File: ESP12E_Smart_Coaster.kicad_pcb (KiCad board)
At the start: 2 copper layers, 110.7 x 110.7 mm, 49 parts, among them J1 SPI_Header, J2 MLX90614 Temp Sensor, J3 Programming_header, J4 Power_Input_Header, Q1 SI2302, SW1 SW_SPDT, SW2 SW_Push, U1 T6845C_Module, U2 AMS1117-3.3, U3 ESP-12E

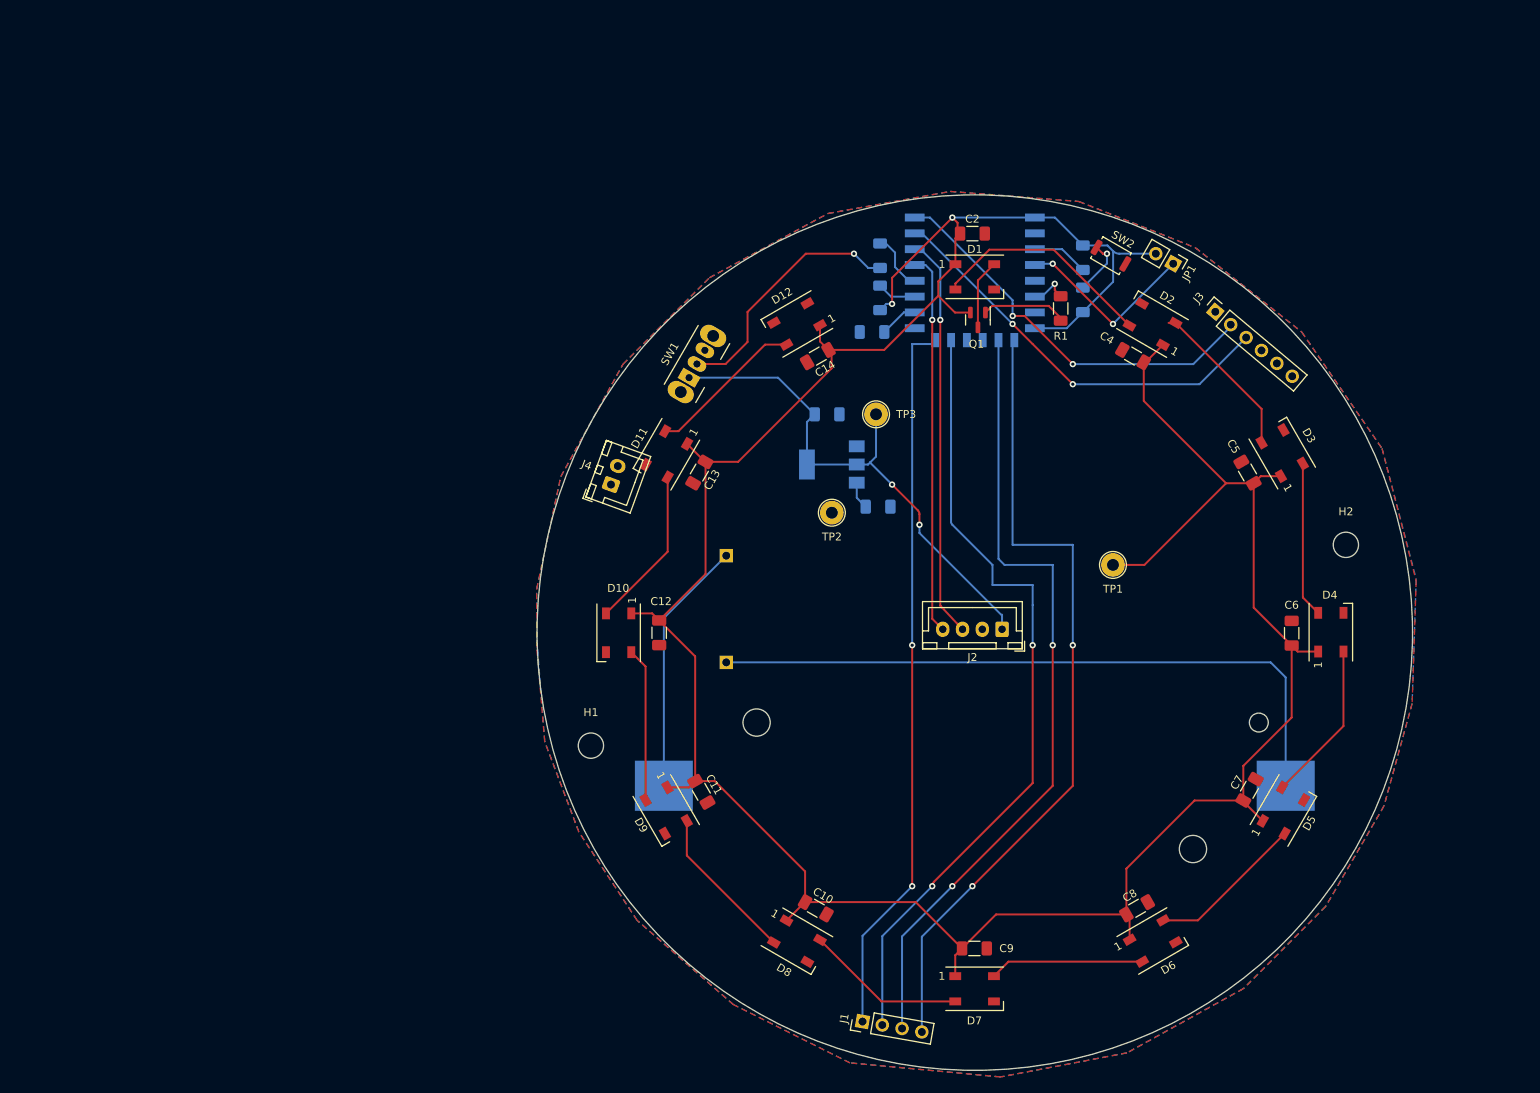
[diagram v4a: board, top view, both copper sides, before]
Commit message: Changed connector positions
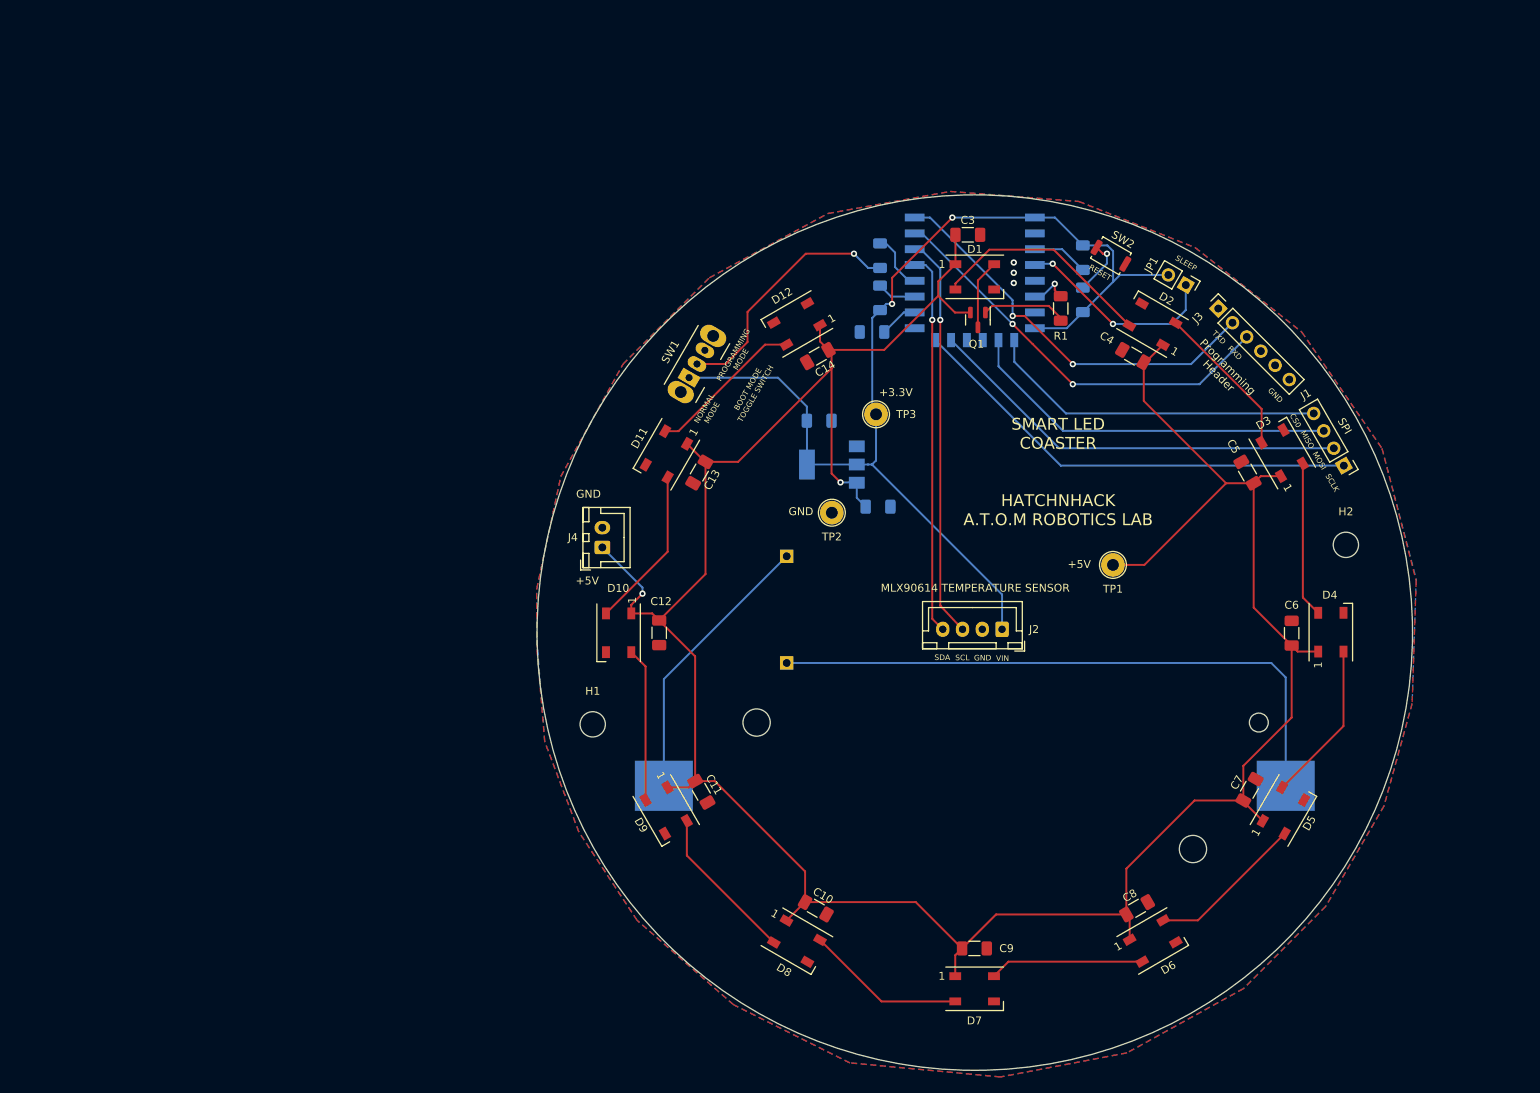
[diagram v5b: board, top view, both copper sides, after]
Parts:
- C2: moved to B.Cu
- C3: moved to F.Cu
- moved J1 93.0 mm to (186.7, 78.9), turned to -150 degrees
- moved C2 30.6 mm to (120.3, 73.2)
- moved C3 28.9 mm to (139.1, 49.7)
- moved J4 8.02 mm to (92.9, 89.2), turned to 90 degrees
- moved U1 7.65 mm to (106.7, 96.6)
- moved JP1 3.13 mm to (166.7, 56.0)
- moved H1 2.70 mm to (91.7, 111.6)
- moved J3 0.55 mm to (170.8, 59.0), turned to 45 degrees
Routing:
- net CS0: track 103.1 -> 43.3 mm, vias 2 -> 0
- net MISO: track 101.4 -> 47.8 mm, vias 2 -> 0
- net MOSI: track 101.7 -> 54.1 mm, vias 2 -> 0
- net SCLK: track 90.8 -> 58.3 mm, vias 2 -> 0
- net +5V: track 319.7 -> 347.3 mm, vias 0 -> 2
- net RESET: track 129.2 -> 141.6 mm, vias 4 -> 2
- net Net-(BT1-Pad1): track 85.3 -> 77.6 mm
- net Net-(BT1-Pad2): track 32.4 -> 35.5 mm
- net WAKE: track 23.9 -> 26.2 mm
- net Net-(D2-Pad2): track 20.5 -> 19.7 mm
- net TXD: track 50.5 -> 51.2 mm
- net GND: vias 0 -> 3
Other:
- board text added: "+3.3V"
- board text added: "+5V"
- board text added: "3.7V 2200 mAH LI-ION CELL"
- board text added: "BOOT MODE TOGGLE SWITCH"
- board text added: "CS0"
- board text added: "GND"
- board text added: "MISO"
- board text added: "MLX90614 TEMPERATURE SENSOR"
- board text added: "MOSI"
- board text added: "NORMAL MODE"
- board text added: "POWER BANK MODULE"
- board text added: "PROGRAMMING MODE"
- board text added: "Programming Header"
- board text added: "RESET"
- board text added: "RXD"
- board text added: "SCL"
- board text added: "SCLK"
- board text added: "SDA"
- board text added: "SLEEP"
- board text added: "SMART LED COASTER HATCHNHACK A.T.O.M ROBOTICS LAB"
- board text added: "SPI"
- board text added: "TXD"
- board text added: "VIN"

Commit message: Added graphics
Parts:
- added C15: 100uF, Capacitor_SMD:C_1206_3216Metric_Pad1.33x1.80mm_HandSolder, F.Cu at (132.1, 66.0)
- moved C3 7.21 mm to (139.1, 56.9)
- moved R5 6.30 mm to (128.0, 58.6)
- moved R6 6.30 mm to (153.7, 64.2)
- moved D1 6.30 mm to (140.0, 61.3)
- moved Q1 6.30 mm to (140.4, 66.8)
- moved R1 6.30 mm to (150.9, 65.3)
- moved R2 6.30 mm to (127.0, 68.3)
- moved R3 6.30 mm to (128.0, 64.0)
- moved R4 6.30 mm to (153.7, 58.9)
- moved U3 6.30 mm to (140.0, 57.3)
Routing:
- net RESET: track 141.6 -> 158.0 mm, vias 2 -> 3
- net SCL: track 51.9 -> 44.6 mm
- net SDA: track 48.4 -> 41.8 mm
- net Net-(R6-Pad2): track 7.19 -> 13.0 mm
- net WAKE: track 26.2 -> 22.3 mm
- net MISO: track 47.8 -> 44.2 mm
- net CS0: track 43.3 -> 39.9 mm
- net Net-(D1-Pad2): track 28.5 -> 25.5 mm
- net +5V: track 347.3 -> 344.5 mm
- net MOSI: track 54.1 -> 52.4 mm
- net SCLK: track 58.3 -> 56.6 mm
- net Net-(Q1-Pad1): track 10.9 -> 9.95 mm
- net LED_DIN: track 5.07 -> 5.86 mm
- net Net-(R5-Pad1): track 31.9 -> 31.3 mm
- net GND: vias 3 -> 0
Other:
- board size 110.7 x 110.7 mm -> 110.8 x 110.2 mm
- board text added: "@a.t.o.m_robotics_lab"
- board text added: "@hatchnhack"
- board text added: "https://atom-robotics-lab.github.io/"
- board text added: "https://www.hnhcart.com/"
- board text removed: "SMART LED COASTER HATCHNHACK A.T.O.M ROBOTICS LAB"

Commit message: Added gerber files
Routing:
- net +5V: track 344.5 -> 350.3 mm
